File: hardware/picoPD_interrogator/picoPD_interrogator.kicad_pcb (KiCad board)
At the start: 2 copper layers, 63.5 x 26 mm, 53 parts, among them J1 Conn_01x07, J2 USB_C_Receptacle_USB2.0_16P, J3 Conn_01x14, Q1 rohm-RE1C002UN, Q2 rohm-RE1C002UN, Q3 rohm-RE1C002UN, Q4 rohm-RE1C002UN, Q5 rohm-RE1C002UN, SW1 RESET_BTN, U1 TCPC, U3 ST-LM393QT, U6 LV2862XDDC

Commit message: PCB: Working on PCB layout.
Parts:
- moved C2 15.5 mm to (161.2, 25.9), turned to -90 degrees
- moved C6 14.7 mm to (156.1, 34.4), turned to -90 degrees
- moved L1 13.1 mm to (156.2, 30.7), turned to -90 degrees
- moved D2 13.0 mm to (157.0, 26.4)
- moved C5 12.2 mm to (157.8, 30.0)
- moved C3 10.6 mm to (159.9, 34.4), turned to -90 degrees
- moved C4 10.5 mm to (158.0, 34.4), turned to -90 degrees
- moved D1 9.49 mm to (163.5, 26.4)
- moved C1 9.24 mm to (159.3, 25.9), turned to -90 degrees
- moved R24 3.65 mm to (161.4, 33.6)
- moved R23 3.18 mm to (162.5, 33.6)
- moved R20 1.25 mm to (163.1, 29.3), turned to 0 degrees

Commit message: PCB: Working on PCB layout.
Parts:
- TP1: footprint TestPoint:TestPoint_Pad_D4.0mm -> TestPoint:TestPoint_Pad_D2.5mm
- U1: value TCPC -> ~
- moved C1 102.2 mm to (118.5, 119.7)
- moved C2 102.2 mm to (120.5, 119.7)
- moved C3 102.2 mm to (119.2, 128.1)
- moved C4 102.2 mm to (117.2, 128.1)
- moved C5 102.2 mm to (117.0, 123.7)
- moved C6 102.2 mm to (115.3, 128.1)
- moved L1 102.2 mm to (115.5, 124.4)
- moved R20 102.2 mm to (122.3, 123.0)
- moved U6 102.2 mm to (119.5, 123.7)
- moved D1 102.2 mm to (122.8, 120.0)
- moved D2 102.2 mm to (116.2, 120.0)
- moved R23 102.2 mm to (121.8, 127.3)
- moved R24 102.2 mm to (120.7, 127.3)
- moved SW1 78.2 mm to (140.9, 109.6), turned to -90 degrees
- moved R1 78.1 mm to (170.6, 59.6)
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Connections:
- net Net-(J2-D+-PadA6) renamed /USB_DP_CONN
- net Net-(J2-D--PadA7) renamed /USB_DM_CONN
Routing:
- net /USB_DM_CONN: track 0.00 -> 2.34 mm
- net /USB_DP_CONN: track 0.00 -> 2.34 mm
- net GND: vias 0 -> 1

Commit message: PCB: Working on PCB layout.
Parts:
- moved R23 40.1 mm to (132.8, 88.8), turned to 180 degrees
- moved C3 39.4 mm to (133.6, 91.5), turned to 0 degrees
- moved R24 39.3 mm to (132.8, 90.0), turned to 180 degrees
- moved C4 38.4 mm to (133.6, 93.3), turned to 0 degrees
- moved C6 37.6 mm to (133.6, 95.2), turned to 0 degrees
- moved R20 35.2 mm to (128.4, 88.3), turned to 90 degrees
- moved U6 34.0 mm to (129.2, 91.1), turned to 180 degrees
- moved L1 32.6 mm to (129.8, 95.2), turned to 0 degrees
- moved C5 32.5 mm to (129.2, 93.5), turned to 180 degrees
- moved C2 29.9 mm to (125.1, 90.2), turned to 0 degrees
- moved D1 29.3 mm to (121.3, 90.8), turned to -90 degrees
- moved C1 28.4 mm to (125.1, 92.0), turned to 0 degrees
- moved D2 27.3 mm to (125.5, 94.3), turned to 180 degrees
- moved TP1 16.7 mm to (118.2, 91.0)

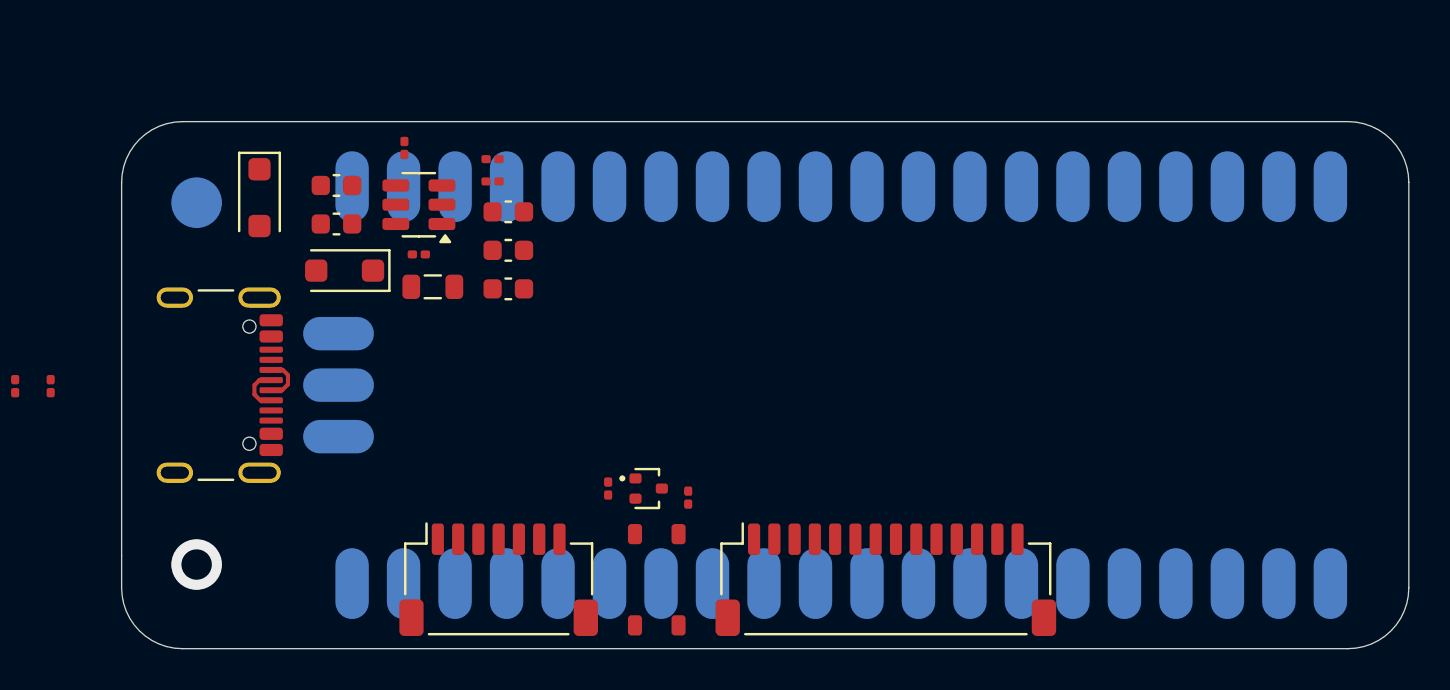
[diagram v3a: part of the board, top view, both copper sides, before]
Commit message: PCB: Added first copper layer.
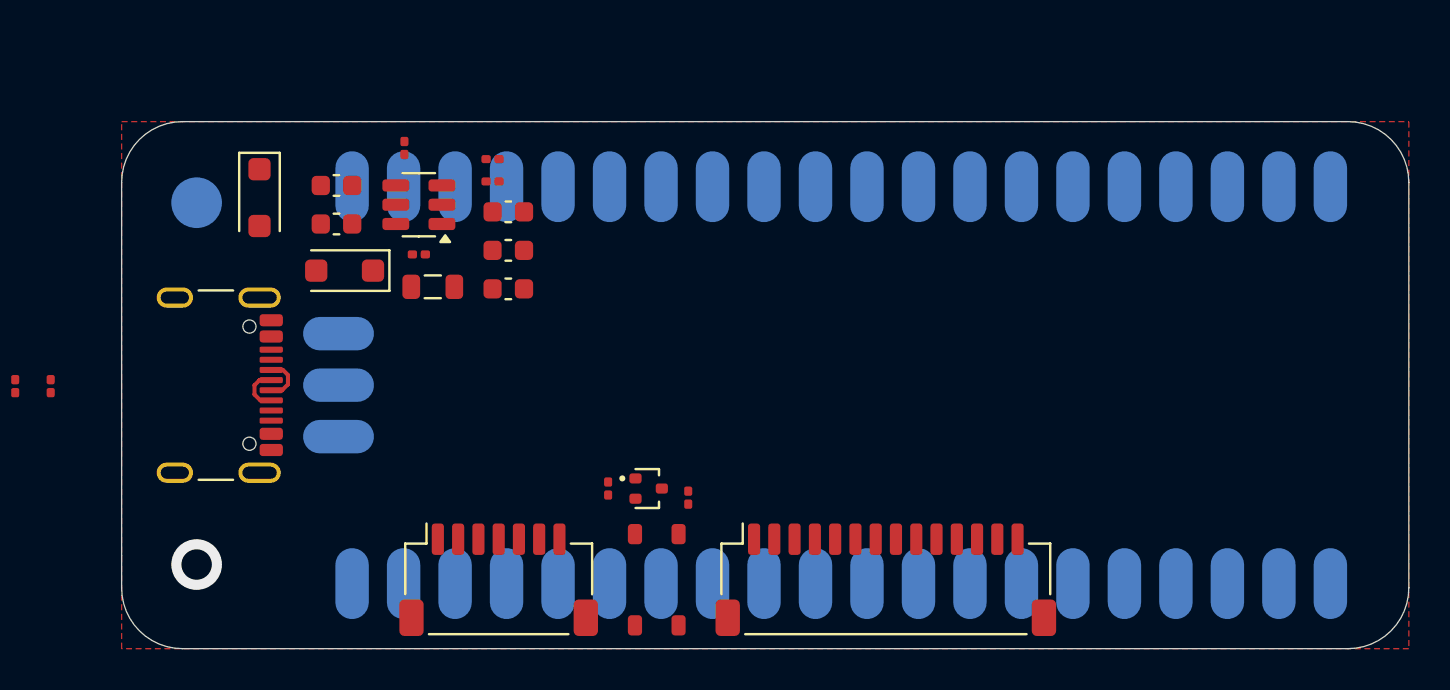
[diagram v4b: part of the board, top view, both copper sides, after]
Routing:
- added copper zone on F.Cu, net GND
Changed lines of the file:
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@@
 		(net 8)
+	)
+	(zone
+		(net 1)
+		(net_name "GND")
+		(layer "F.Cu")
+		(hatch edge 0.5)
+		(connect_pads
+			(clearance 0.25)
+		)
+		(min_thickness 0.25)
+		(filled_areas_thickness no)
+		(fill yes
+			(thermal_gap 0.5)
+			(thermal_bridge_width 0.5)
+		)
+		(polygon
+			(pts
+				(xy 114.5 87) (xy 178 87) (xy 178 113) (xy 114.5 113)
+			)
+		)
 	)
 	(embedded_fonts no)

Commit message: PCB: Working on board layout.
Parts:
- added R29: 3.3K, Resistor_SMD:R_0201_0603Metric, F.Cu at (156.8, 104.4)
- moved R7 52.1 mm to (137.4, 93.6), turned to 0 degrees
- moved R16 52.0 mm to (164.9, 90.2), turned to -90 degrees
- moved U1 51.3 mm to (137.7, 95.5), turned to 0 degrees
- moved Q5 48.9 mm to (163.0, 90.6), turned to 180 degrees
- moved R2 47.9 mm to (155.8, 104.4)
- moved R1 47.6 mm to (154.7, 104.4)
- moved R17 46.4 mm to (165.8, 106.7), turned to 0 degrees
- moved R19 45.1 mm to (159.7, 92.5), turned to 180 degrees
- moved Q4 43.9 mm to (160.2, 90.6), turned to 180 degrees
- moved R18 43.6 mm to (162.5, 105.2), turned to -90 degrees
- moved R11 42.3 mm to (149.4, 90.2), turned to -90 degrees
- moved R15 40.1 mm to (158.2, 90.2), turned to -90 degrees
- moved Q2 40.1 mm to (147.5, 90.6), turned to 180 degrees
- moved R3 39.4 mm to (156.6, 91.9), turned to 90 degrees
- moved R13 38.8 mm to (144.2, 92.5), turned to 180 degrees
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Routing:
- net /GP15: track 0.00 -> 41.4 mm, vias 0 -> 3
- net /GP16: track 0.00 -> 40.5 mm, vias 0 -> 3
- net /GP17: track 0.00 -> 33.1 mm, vias 0 -> 1
- net /GP18: track 0.00 -> 27.4 mm, vias 0 -> 1
- net /GP19: track 0.00 -> 25.6 mm, vias 0 -> 1
- net /SDA: track 0.00 -> 25.1 mm, vias 0 -> 1
- net /SCL: track 0.00 -> 24.1 mm, vias 0 -> 1
- net /SPI0_CLK: track 0.00 -> 23.1 mm, vias 0 -> 2
- net /TCPC_INT: track 0.00 -> 21.9 mm, vias 0 -> 1
- net /SPI0_MOSI: track 0.00 -> 19.2 mm, vias 0 -> 2
- net /SWD_CLK: track 0.00 -> 16.0 mm, vias 0 -> 1
- net /SPI0_MISO: track 0.00 -> 15.2 mm, vias 0 -> 2
- net /3V3: track 0.00 -> 13.3 mm, vias 0 -> 3
- net /PIO_USB_DP: track 0.00 -> 12.8 mm, vias 0 -> 1
- net /USB_DM_CONN: track 2.34 -> 13.7 mm
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- added copper zone on B.Cu, net /VBUS_CONN
- added copper zone on In2.Cu, net /VBUS_CONN
- added copper zone on B.Cu, net GND
- added copper zone on In1.Cu, net GND
- added copper zone on In2.Cu, net GND
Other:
- copper layers 2 -> 4

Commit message: PCB: Working on PCB layout.
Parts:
- moved R7 24.0 mm to (159.3, 103.3)
- moved U1 22.8 mm to (159.7, 101.6), turned to 180 degrees
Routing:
- net /3V3: track 13.3 -> 31.2 mm, vias 3 -> 8
- net /GP28_A2: track 0.00 -> 17.2 mm, vias 0 -> 2
- net /CC1_CONN: track 7.63 -> 23.5 mm, vias 1 -> 4
- net /CC2_CONN: track 7.63 -> 20.4 mm, vias 1 -> 3
- net GND: track 3.98 -> 13.0 mm, vias 14 -> 15
- net /BMC_VREF: track 0.00 -> 8.17 mm, vias 0 -> 2
- net /CC1_VCONN_EN: track 0.00 -> 4.87 mm, vias 0 -> 1
- net /CC2_TX: track 0.00 -> 4.72 mm
- net /CC1_TX: track 0.00 -> 4.45 mm
- net /CC2_VCONN_EN: track 0.00 -> 3.64 mm, vias 0 -> 1
- net Net-(U4-B2): track 0.00 -> 3.58 mm
- net Net-(U5-B2): track 0.00 -> 3.57 mm
- net Net-(Q1-D): track 0.00 -> 1.62 mm
- net Net-(Q4-D): track 0.00 -> 1.62 mm
- net /CC1_RX: track 0.00 -> 1.44 mm
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
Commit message: PCB: Working on PCB layout.
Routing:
- net /3V3: track 31.2 -> 31.3 mm, vias 8 -> 9
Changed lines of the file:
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@@
+	)
+	(segment
+		(start 131.85 95.25)
+		(end 132.8 95.25)
+		(width 0.3)
+		(layer "F.Cu")
+		(net 3)
 	)
 	(segment
@@
 	)
 	(segment
+		(start 130.9125 95.15)
+		(end 131.75 95.15)
+		(width 0.3)
+		(layer "F.Cu")
+		(net 3)
+	)
+	(segment
 		(start 141.05 91.63)
 		(end 141.05 90.47)
@@
 	)
 	(segment
-		(start 156.55 90.455)
-		(end 156.55 91.615)
-		(width 0.2)
+		(start 131.75 95.15)
+		(end 131.85 95.25)
+		(width 0.3)
 		(layer "F.Cu")
 		(net 3)
 	)
 	(segment
-		(start 132.8 95.25)
-		(end 131.0125 95.25)
-		(width 0.3)
+		(start 156.55 90.455)
+		(end 156.55 91.615)
+		(width 0.2)
 		(layer "F.Cu")
 		(net 3)
@@
 		(size 0.6)
 		(drill 0.3)
+		(layers "F.Cu" "B.Cu")
+		(free yes)
+		(net 3)
+	)
+	(via
+		(at 131.85 95.25)
+		(size 0.6)
+		(drill 0.3)

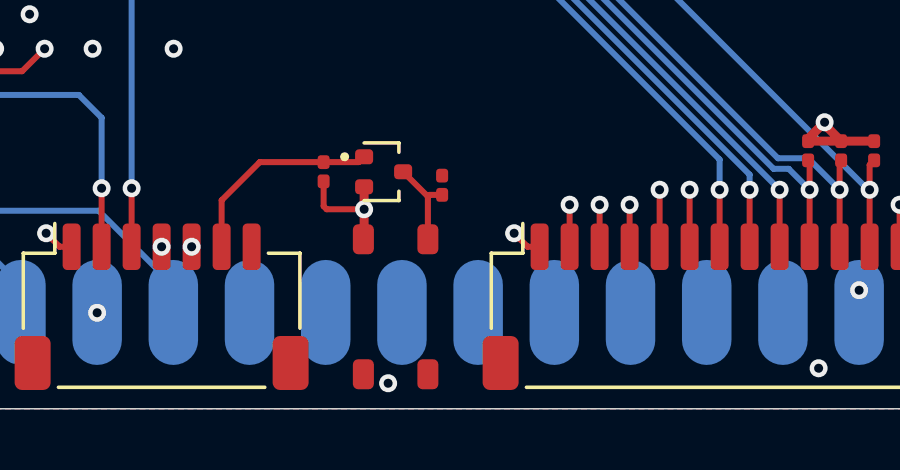
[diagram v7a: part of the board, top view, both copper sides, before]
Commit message: PCB/Schematic: Added JST connector pins to the GND netlist.
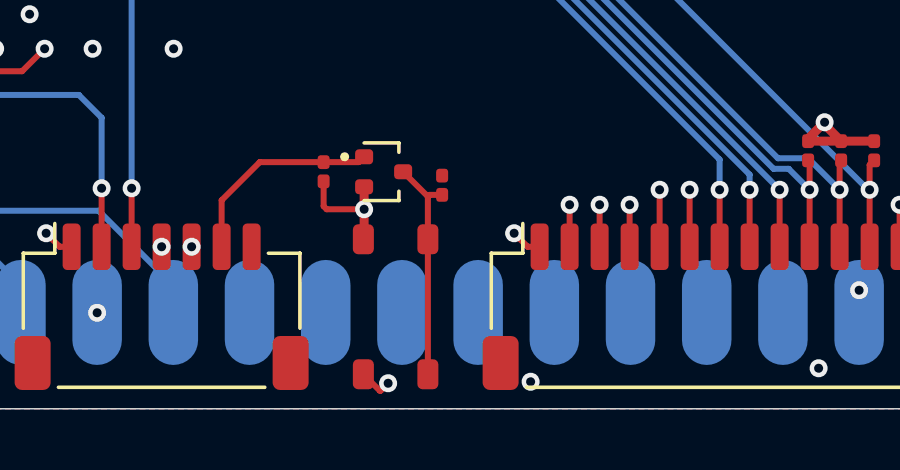
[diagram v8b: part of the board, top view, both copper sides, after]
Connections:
- J1 pad MP: (no net) -> GND
- J3 pad MP: (no net) -> GND
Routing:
- net Net-(Q3-D): track 3.09 -> 7.59 mm
- net GND: track 13.0 -> 14.1 mm, vias 15 -> 16
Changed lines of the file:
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@@
 			(layers "F.Cu" "F.Mask" "F.Paste")
 			(roundrect_rratio 0.208333)
+			(net 1 "GND")
+			(pinfunction "MP")
+			(pintype "passive")
 		)
 		(pad "MP" smd roundrect
@@
 			(layers "F.Cu" "F.Mask" "F.Paste")
 			(roundrect_rratio 0.208333)
+			(net 1 "GND")
+			(pinfunction "MP")
+			(pintype "passive")
 		)
 		(embedded_fonts no)
@@
 			(layers "F.Cu" "F.Mask" "F.Paste")
 			(roundrect_rratio 0.208333)
+			(net 1 "GND")
+			(pinfunction "MP")
+			(pintype "passive")
 		)
 		(pad "MP" smd roundrect
@@
 			(layers "F.Cu" "F.Mask" "F.Paste")
 			(roundrect_rratio 0.208333)
+			(net 1 "GND")
+			(pinfunction "MP")
+			(pintype "passive")
 		)
 		(embedded_fonts no)
@@
 	)
 	(segment
+		(start 140.4 112.4)
+		(end 140.65 112.15)
+		(width 0.2)
+		(layer "F.Cu")
+		(net 1)
+	)
+	(segment
 		(start 138.5 106.25)
 		(end 138.5 105.42)
@@
 	)
 	(segment
+		(start 140.375 112.4)
+		(end 140.4 112.4)
+		(width 0.2)
+		(layer "F.Cu")
+		(net 1)
+	)
+	(segment
 		(start 164.8825 104.5775)
 		(end 164.8825 103.4175)
@@
 	)
 	(segment
+		(start 139.825 111.85)
+		(end 140.375 112.4)
+		(width 0.2)
+		(layer "F.Cu")
+		(net 1)
+	)
+	(segment
 		(start 139.85 107.325)
 		(end 139.825 107.35)
@@
 	)
 	(via
+		(at 145.4 112.1)
+		(size 0.6)
+		(drill 0.3)
+		(layers "F.Cu" "B.Cu")
+		(free yes)
+		(net 1)
+	)
+	(via
 		(at 140.65 112.15)
 		(size 0.6)
@@
 		(width 0.2)
 		(layer "F.Cu")
+		(net 36)
+	)
+	(segment
+		(start 141.975 107.35)
+		(end 141.975 111.85)
+		(width 0.2)
+		(layer "F.Cu")
